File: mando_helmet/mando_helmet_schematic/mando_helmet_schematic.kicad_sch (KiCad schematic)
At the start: 1 part

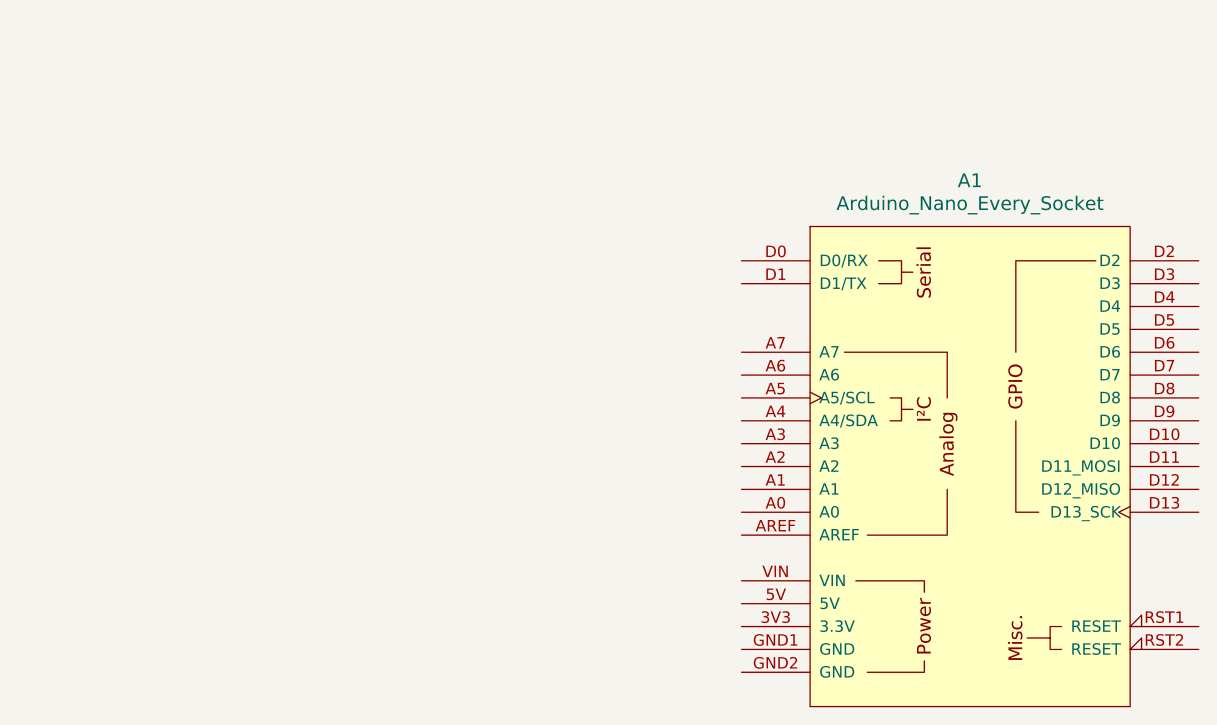
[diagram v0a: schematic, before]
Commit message: move schematic images to respective module folder, update arduino symbol on mando_helmet
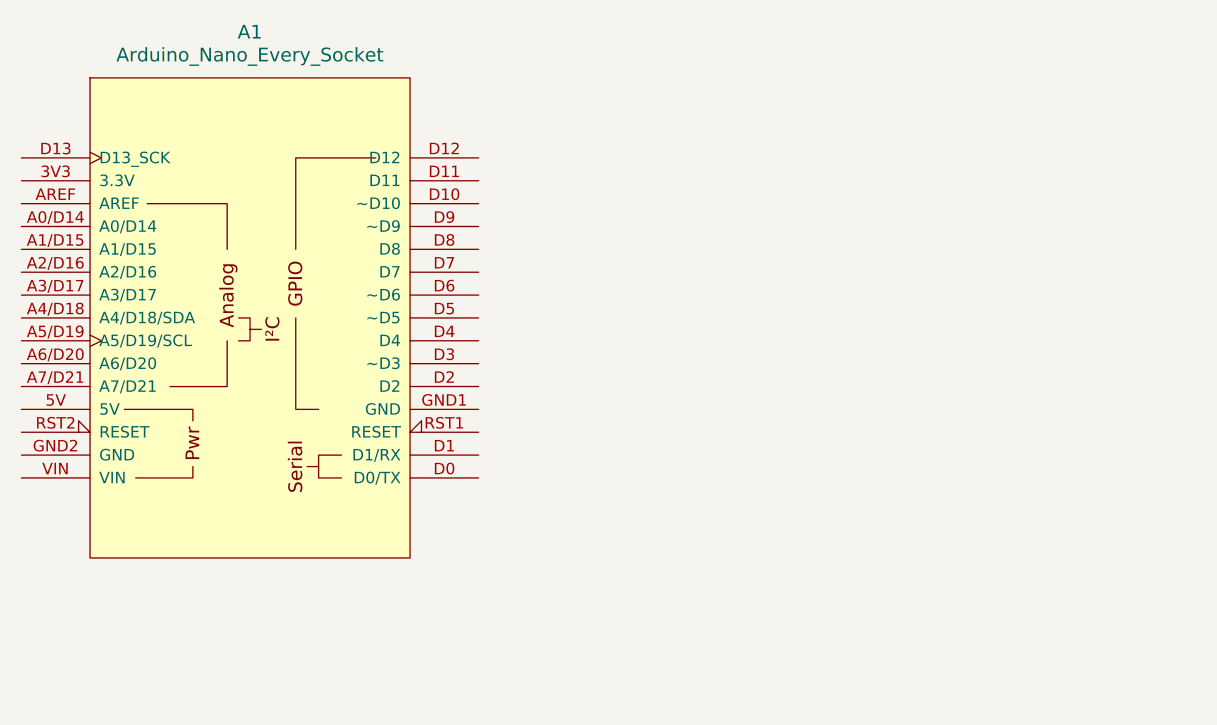
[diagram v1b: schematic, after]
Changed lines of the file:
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@@
 	(symbol
 		(lib_id "PCM_arduino-library:Arduino_Nano_Every_Socket")
-		(at 144.78 82.55 0)
+		(at 64.77 66.04 0)
 		(unit 1)
 		(body_style 1)
@@
 		(fields_autoplaced yes)
 		(property "Reference" "A1"
-			(at 144.78 50.8 0)
+			(at 64.77 34.29 0)
 			(show_name no)
 			(do_not_autoplace no)
@@
 		)
 		(property "Value" "Arduino_Nano_Every_Socket"
-			(at 144.78 53.34 0)
+			(at 64.77 36.83 0)
 			(show_name no)
 			(do_not_autoplace no)
@@
 		)
 		(property "Footprint" "PCM_arduino-library:Arduino_Nano_Every_Socket"
-			(at 144.78 116.84 0)
+			(at 64.77 100.33 0)
 			(hide yes)
 			(show_name no)
@@
 		)
 		(property "Datasheet" "https://docs.arduino.cc/hardware/nano-every"
-			(at 144.78 113.03 0)
+			(at 64.77 96.52 0)
 			(hide yes)
 			(show_name no)
@@
 		)
 		(property "Description" "Socket for Arduino Nano Every"
-			(at 144.78 82.55 0)
+			(at 65.024 64.77 0)
 			(hide yes)
 			(show_name no)
@@
 			)
 		)
-		(pin "3V3"
-		)
-		(pin "A0"
-		)
-		(pin "A3"
-		)
-		(pin "A5"
-		)
-		(pin "A7"
-		)
-		(pin "D0"
+		(pin "D4"
 		)
 		(pin "5V"
-		)
-		(pin "A1"
-		)
-		(pin "A2"
-		)
-		(pin "A4"
-		)
-		(pin "A6"
-		)
-		(pin "AREF"
-		)
-		(pin "D6"
-		)
-		(pin "D13"
-		)
-		(pin "D1"
-		)
-		(pin "D11"
-		)
-		(pin "D10"
-		)
-		(pin "D12"
-		)
-		(pin "GND1"
-		)
-		(pin "D8"
-		)
-		(pin "GND2"
-		)
-		(pin "D9"
 		)
 		(pin "D2"
@@
 		(pin "D7"
 		)
-		(pin "D4"
+		(pin "A3/D17"
 		)
-		(pin "D3"
+		(pin "A0/D14"
+		)
+		(pin "~D6"
+		)
+		(pin "~D5"
+		)
+		(pin "A2/D16"
+		)
+		(pin "GND2"
+		)
+		(pin "A4/D18"
+		)
+		(pin "~D9"
+		)
+		(pin "D12"
+		)
+		(pin "VIN"
+		)
+		(pin "A6/D20"
+		)
+		(pin "D1"
+		)
+		(pin "GND1"
+		)
+		(pin "D0"
+		)
+		(pin "A7/D21"
+		)
+		(pin "AREF"
+		)
+		(pin "A5/D19"
+		)
+		(pin "3V3"
+		)
+		(pin "A1/D15"
+		)
+		(pin "D8"
+		)
+		(pin "D11"
+		)
+		(pin "D13"
 		)
 		(pin "RST1"
 		)
-		(pin "D5"
-		)
-		(pin "VIN"
-		)
 		(pin "RST2"
 		)
+		(pin "~D3"
+		)
+		(pin "~D10"
+		)
 		(instances
